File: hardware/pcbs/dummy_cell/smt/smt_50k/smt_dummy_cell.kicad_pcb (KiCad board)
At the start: 2 copper layers, 8.6 x 25 mm, 2 parts, among them J1 Conn_01x03

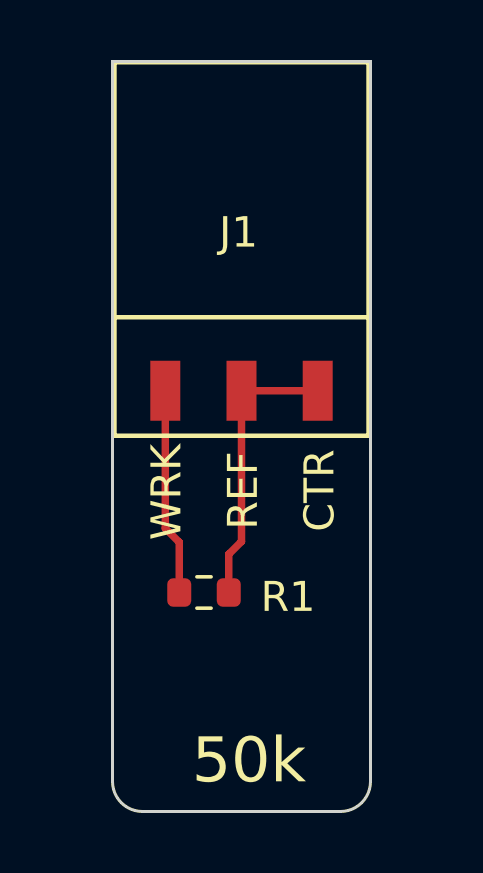
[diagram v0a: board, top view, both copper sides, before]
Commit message: Made new smt dummy cell pcb slight wider for assembly.
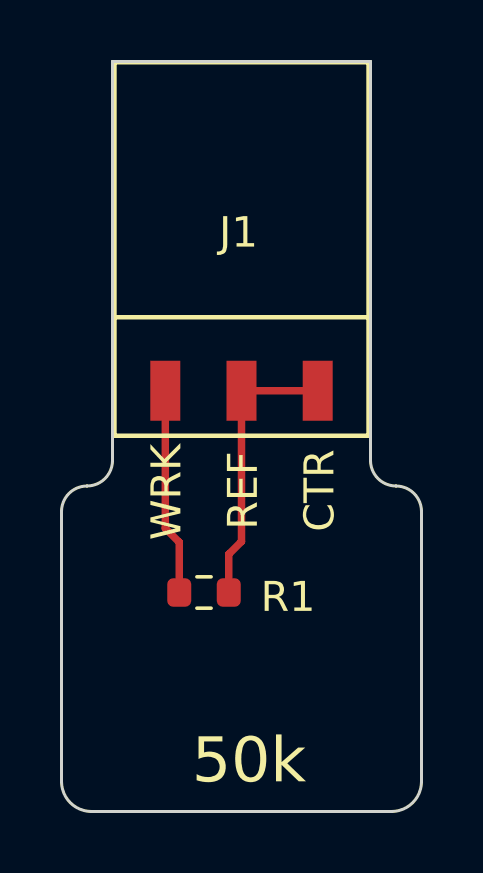
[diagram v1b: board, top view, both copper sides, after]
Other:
- board size 8.6 x 25 mm -> 12 x 25 mm
- board text added: "Dummy Cell V0.2 R2"
- board text removed: "Dummy Cell V0.2 R1"
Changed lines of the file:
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@@
   (general
     (thickness 1.6)
-    (drawings 12)
+    (drawings 18)
     (tracks 7)
     (zones 0)
@@
   (module GCT_BG300:BG300_03 (layer F.Cu)
     (at 55 56.25)
+    (attr smd)
     (fp_text reference J1 (at -0.1 -0.55) (layer F.SilkS)
       (effects (font (size 1.016 1.016) (thickness 0.2032)))
@@
     (fp_line (start 4.235 -6.225) (end 4.235 6.225) (layer F.SilkS) (width 0.15))
     (fp_line (start -4.235 -6.225) (end -4.235 6.225) (layer F.SilkS) (width 0.15))
+    (pad 3 smd rect (at 2.54 4.725) (size 1 2) (layers F.Cu F.Paste F.Mask)
+      (net 2 /CTR))
+    (pad 2 smd rect (at 0 4.725) (size 1 2) (layers F.Cu F.Paste F.Mask)
+      (net 2 /CTR))
     (pad 1 smd rect (at -2.54 4.725) (size 1 2) (layers F.Cu F.Paste F.Mask)
       (net 1 /WRK))
-    (pad 2 smd rect (at 0 4.725) (size 1 2) (layers F.Cu F.Paste F.Mask)
-      (net 2 /CTR))
-    (pad 3 smd rect (at 2.54 4.725) (size 1 2) (layers F.Cu F.Paste F.Mask)
-      (net 2 /CTR))
   )
   (module Resistor_SMD:R_0603_1608Metric (layer F.Cu)
@@
       (effects (font (size 1 1) (thickness 0.15)))
     )
+    (fp_line (start -0.8 0.4125) (end -0.8 -0.4125) (layer F.Fab) (width 0.1))
+    (fp_line (start -0.8 -0.4125) (end 0.8 -0.4125) (layer F.Fab) (width 0.1))
+    (fp_line (start 0.8 -0.4125) (end 0.8 0.4125) (layer F.Fab) (width 0.1))
+    (fp_line (start 0.8 0.4125) (end -0.8 0.4125) (layer F.Fab) (width 0.1))
+    (fp_line (start -0.237258 -0.5225) (end 0.237258 -0.5225) (layer F.SilkS) (width 0.12))
+    (fp_line (start -0.237258 0.5225) (end 0.237258 0.5225) (layer F.SilkS) (width 0.12))
+    (fp_line (start -1.48 0.73) (end -1.48 -0.73) (layer F.CrtYd) (width 0.05))
+    (fp_line (start -1.48 -0.73) (end 1.48 -0.73) (layer F.CrtYd) (width 0.05))
+    (fp_line (start 1.48 -0.73) (end 1.48 0.73) (layer F.CrtYd) (width 0.05))
     (fp_line (start 1.48 0.73) (end -1.48 0.73) (layer F.CrtYd) (width 0.05))
-    (fp_line (start 1.48 -0.73) (end 1.48 0.73) (layer F.CrtYd) (width 0.05))
-    (fp_line (start -1.48 -0.73) (end 1.48 -0.73) (layer F.CrtYd) (width 0.05))
-    (fp_line (start -1.48 0.73) (end -1.48 -0.73) (layer F.CrtYd) (width 0.05))
-    (fp_line (start -0.237258 0.5225) (end 0.237258 0.5225) (layer F.SilkS) (width 0.12))
-    (fp_line (start -0.237258 -0.5225) (end 0.237258 -0.5225) (layer F.SilkS) (width 0.12))
-    (fp_line (start 0.8 0.4125) (end -0.8 0.4125) (layer F.Fab) (width 0.1))
-    (fp_line (start 0.8 -0.4125) (end 0.8 0.4125) (layer F.Fab) (width 0.1))
-    (fp_line (start -0.8 -0.4125) (end 0.8 -0.4125) (layer F.Fab) (width 0.1))
-    (fp_line (start -0.8 0.4125) (end -0.8 -0.4125) (layer F.Fab) (width 0.1))
     (fp_text user %R (at 0 0) (layer F.Fab)
       (effects (font (size 0.4 0.4) (thickness 0.06)))
@@
     )
   )
-  (gr_arc (start 58.3 74) (end 58.3 75) (angle -90) (layer Edge.Cuts) (width 0.1))
-  (gr_arc (start 51.7 74) (end 50.7 74) (angle -90) (layer Edge.Cuts) (width 0.1))
+  (gr_line (start 59.3 50) (end 59.3 63.3) (layer Edge.Cuts) (width 0.1))
+  (gr_line (start 50.7 50) (end 50.7 63.3) (layer Edge.Cuts) (width 0.1))
+  (gr_line (start 61 65) (end 61 74) (layer Edge.Cuts) (width 0.1))
+  (gr_line (start 49 65) (end 49 74) (layer Edge.Cuts) (width 0.1))
+  (gr_arc (start 60.15 63.3) (end 59.3 63.3) (angle -90) (layer Edge.Cuts) (width 0.1))
+  (gr_arc (start 60.15 65) (end 61 65) (angle -90) (layer Edge.Cuts) (width 0.1))
+  (gr_arc (start 49.85 63.3) (end 49.85 64.15) (angle -90) (layer Edge.Cuts) (width 0.1))
+  (gr_arc (start 49.85 65) (end 49.85 64.15) (angle -90) (layer Edge.Cuts) (width 0.1))
+  (gr_line (start 50 75) (end 60 75) (layer Edge.Cuts) (width 0.1))
+  (gr_arc (start 60 74) (end 60 75) (angle -90) (layer Edge.Cuts) (width 0.1))
+  (gr_arc (start 50 74) (end 49 74) (angle -90) (layer Edge.Cuts) (width 0.1))
   (gr_text 50k (at 55.25 73.3) (layer F.SilkS)
     (effects (font (size 1.5 1.5) (thickness 0.25)))
@@
     (effects (font (size 1 1) (thickness 0.15)) (justify mirror))
   )
-  (gr_text "Dummy Cell V0.2 R1" (at 53.75 62.5 90) (layer B.SilkS)
+  (gr_text "Dummy Cell V0.2 R2" (at 53.75 62.5 90) (layer B.SilkS)
     (effects (font (size 1 1) (thickness 0.15)) (justify mirror))
   )
-  (gr_line (start 58.3 75) (end 51.7 75) (layer Edge.Cuts) (width 0.1))
-  (gr_line (start 59.3 50) (end 59.3 74) (layer Edge.Cuts) (width 0.1))
   (gr_line (start 50.7 50) (end 59.3 50) (layer Edge.Cuts) (width 0.1))
-  (gr_line (start 50.7 50) (end 50.7 74) (layer Edge.Cuts) (width 0.1))
   (segment (start 52.46 60.975) (end 52.46 65.56) (width 0.25) (layer F.Cu) (net 1))
   (segment (start 52.925 66.025) (end 52.925 67.7) (width 0.25) (layer F.Cu) (net 1))
